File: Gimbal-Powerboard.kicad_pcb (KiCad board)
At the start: 2 copper layers, 59.7 x 124.9 mm, 169 parts, among them Q1 Q_PMOS_GDS, Q2 Q_PMOS_GDS, Q3 SI4116DY, Q4 SI4116DY, Q5 SI4116DY, Q6 SI4116DY, Q7 SI4116DY, Q8 SI4116DY, U1 DRV8301, U2 NUP4201MR6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

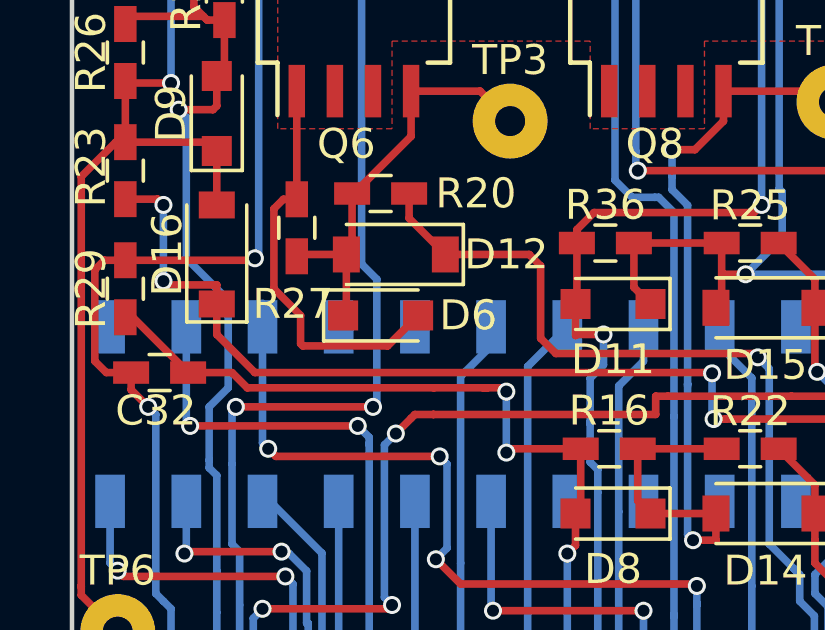
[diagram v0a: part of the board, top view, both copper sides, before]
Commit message: Updated tiva shield with fixed version, generated fresh gerbs
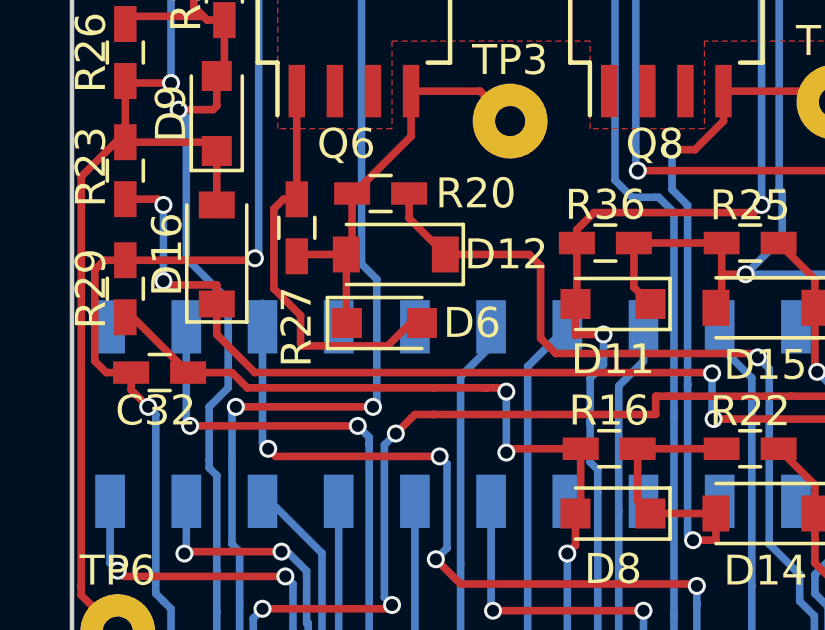
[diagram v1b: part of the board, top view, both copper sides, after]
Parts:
- U3: footprint MRDT_Shields:LAUNCHXL_F28069M_Launchpad_J1_BottomSMD -> MRDT_Shields.pretty:LAUNCHXL_F28069M_Launchpad_J1_BottomSMD
- moved D6 0.28 mm to (123.7, 77.2)

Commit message: Added Atlas Logo!
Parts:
- added G***: LOGO, MRDT_Silkscreens:Atlas_Logo_28.6mmX37.3mm, B.Cu at (156.5, 131.6)
